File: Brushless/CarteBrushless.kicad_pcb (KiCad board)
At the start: 2 copper layers, 60 x 64 mm, 67 parts, among them J1 Conn_01x03_Pin, J2 Conn_01x03_Pin, J3 Conn_01x03_Pin, Q2 IRF7424, U1 STM32G484RETx, U2 TCAN332G

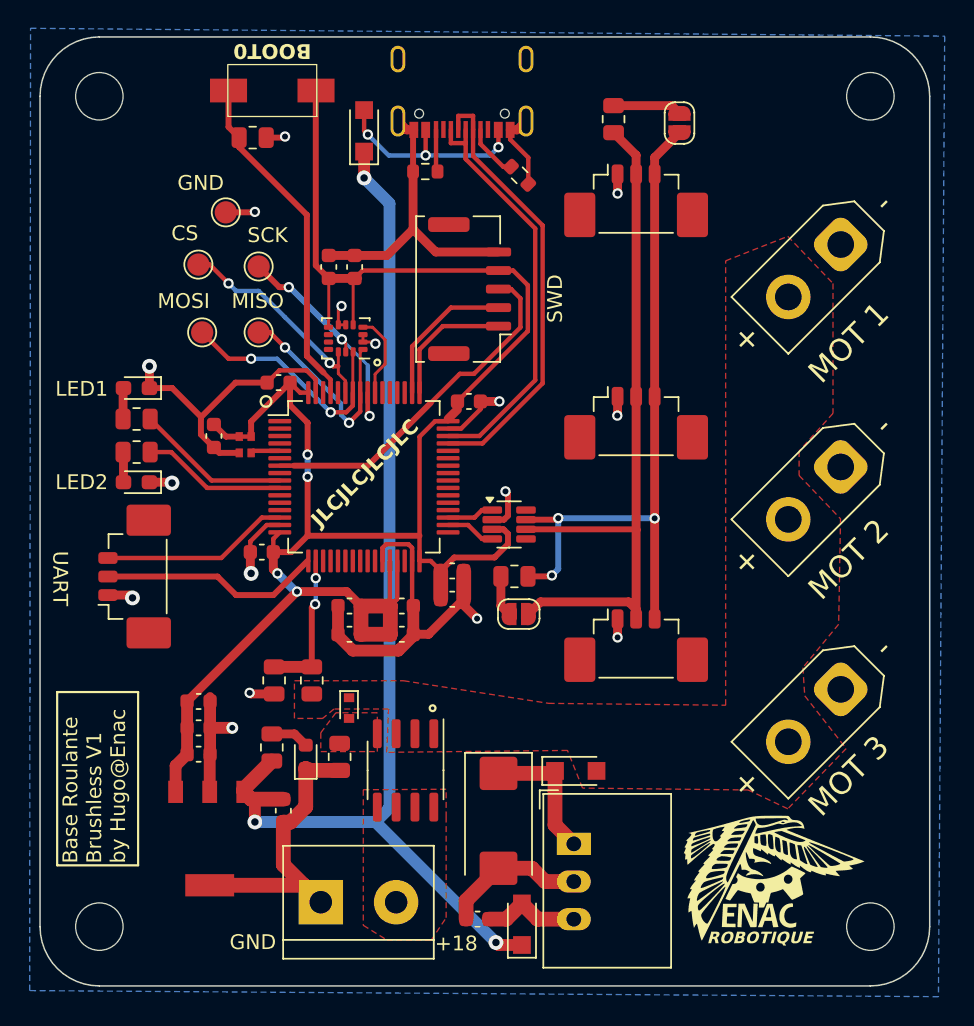
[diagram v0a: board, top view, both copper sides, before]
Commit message: change SWD footprint
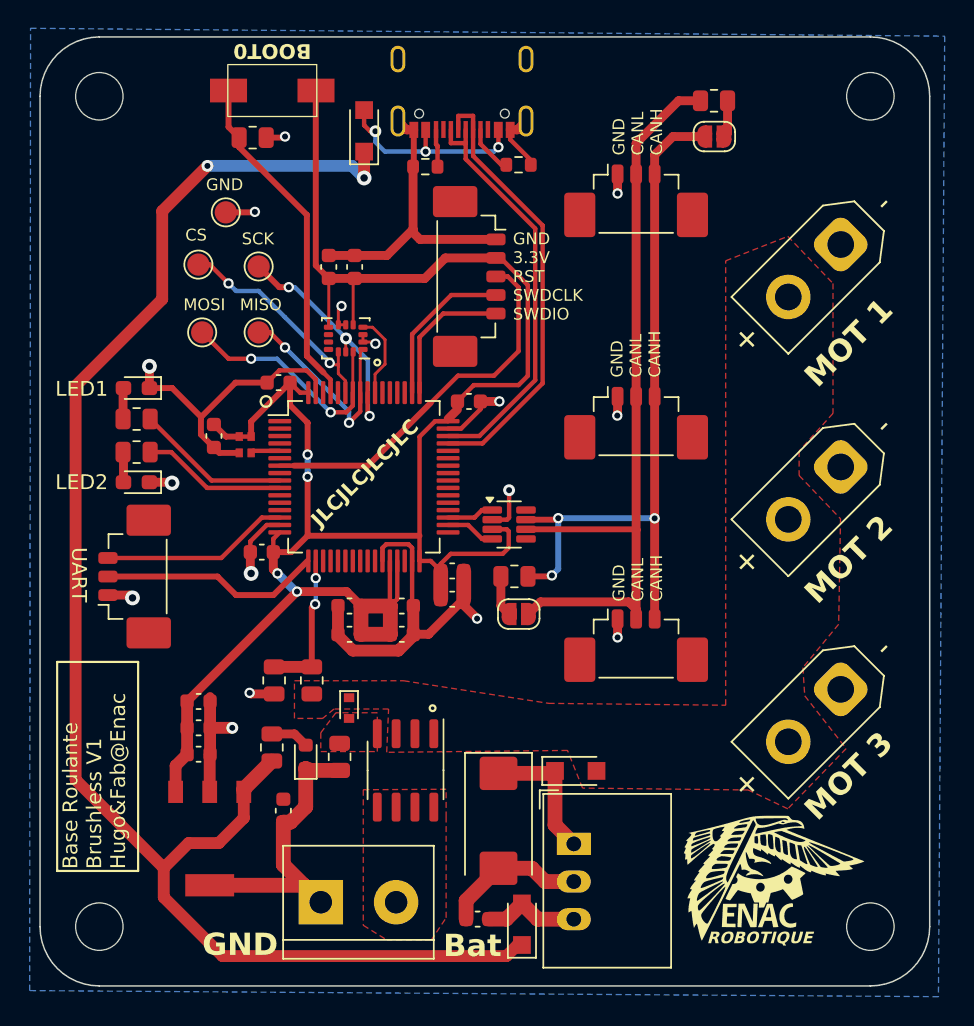
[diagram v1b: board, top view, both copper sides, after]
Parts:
- DEBUG1: footprint Connector_Molex:Molex_CLIK-Mate_502382-0570_1x05-1MP_P1.25mm_Vertical -> Connector_Molex:Molex_PicoBlade_53398-0571_1x05-1MP_P1.25mm_Vertical
- moved R11 6.89 mm to (141.5, 86.5), turned to 0 degrees
- moved JP2 2.52 mm to (141.5, 88.9), turned to 180 degrees
- moved DEBUG1 1.00 mm to (125.5, 98.3), turned to -90 degrees
- moved R7 0.71 mm to (128.3, 90.8), turned to 0 degrees
- moved R8 0.33 mm to (122.0, 90.9)
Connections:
- DEBUG1 pad 1: SWDIO -> GND
- DEBUG1 pad 2: SWCLK -> +3.3V
- DEBUG1 pad 4: +3.3V -> SWCLK
- DEBUG1 pad 5: GND -> SWDIO
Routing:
- net +5V: track 75.1 -> 105.7 mm, vias 3 -> 2
- net CAN_LOW: track 49.3 -> 53.5 mm
- net +3.3V: track 136.7 -> 139.5 mm
- net Net-(JP2-A): track 4.66 -> 2.51 mm
- net CAN_HIGH: track 47.9 -> 49.6 mm
- net RST: track 23.8 -> 25.4 mm
- net GND: track 138.1 -> 136.7 mm
- net SWDIO: track 8.89 -> 9.55 mm
- net SWCLK: track 10.0 -> 10.7 mm
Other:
- board text added: "3.3V"
- board text added: "Base Roulante Brushless V1 Edition 2025 by Hugo&Fab@Enac"
- board text added: "Base Roulante Brushless V1 Hugo&Fab@Enac"
- board text added: "Bat"
- board text added: "CANH"
- board text added: "CANL"
- board text added: "RST"
- board text added: "SWDCLK"
- board text added: "SWDIO"
- board text removed: "+18"
- board text removed: "Base Roulante Brushless V1 Edition 2025 by Hugo@Enac"
- board text removed: "Base Roulante Brushless V1 by Hugo@Enac"
- board text removed: "SWD"

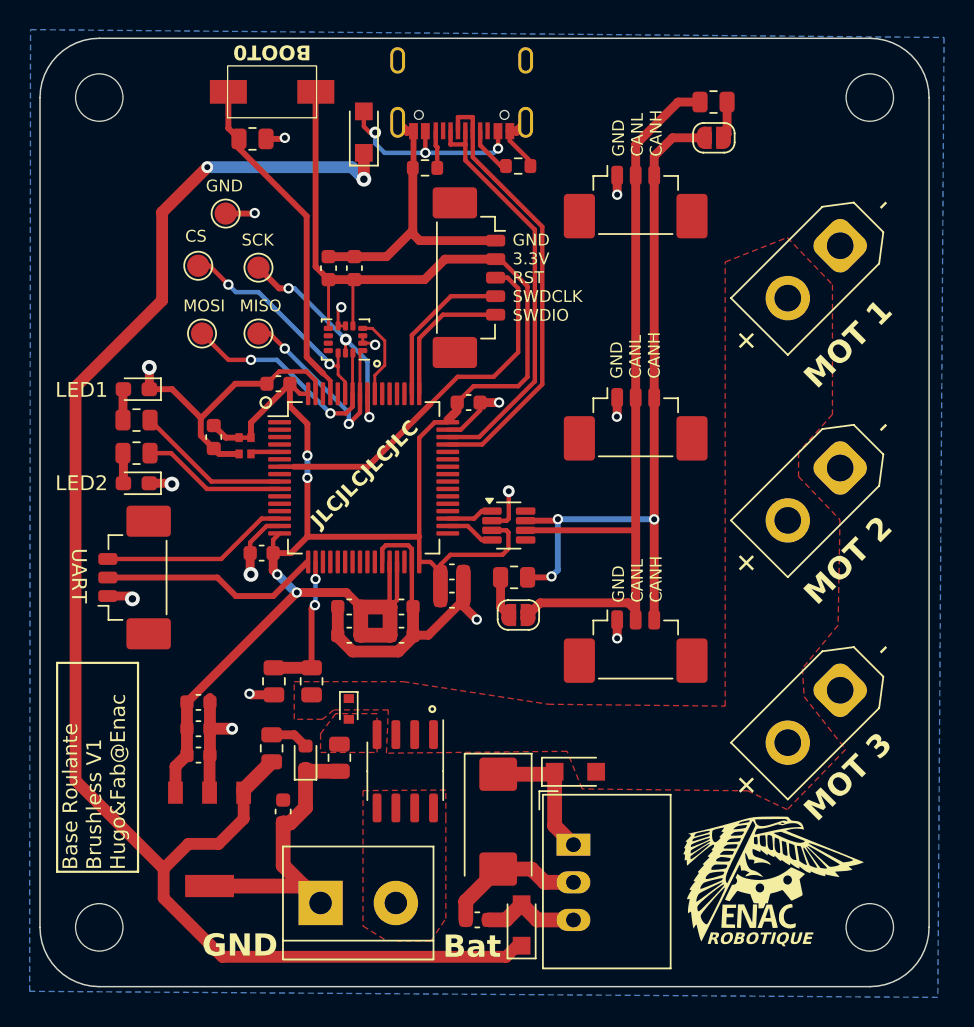
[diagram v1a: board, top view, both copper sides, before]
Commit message: Reduce mounting holes spacing
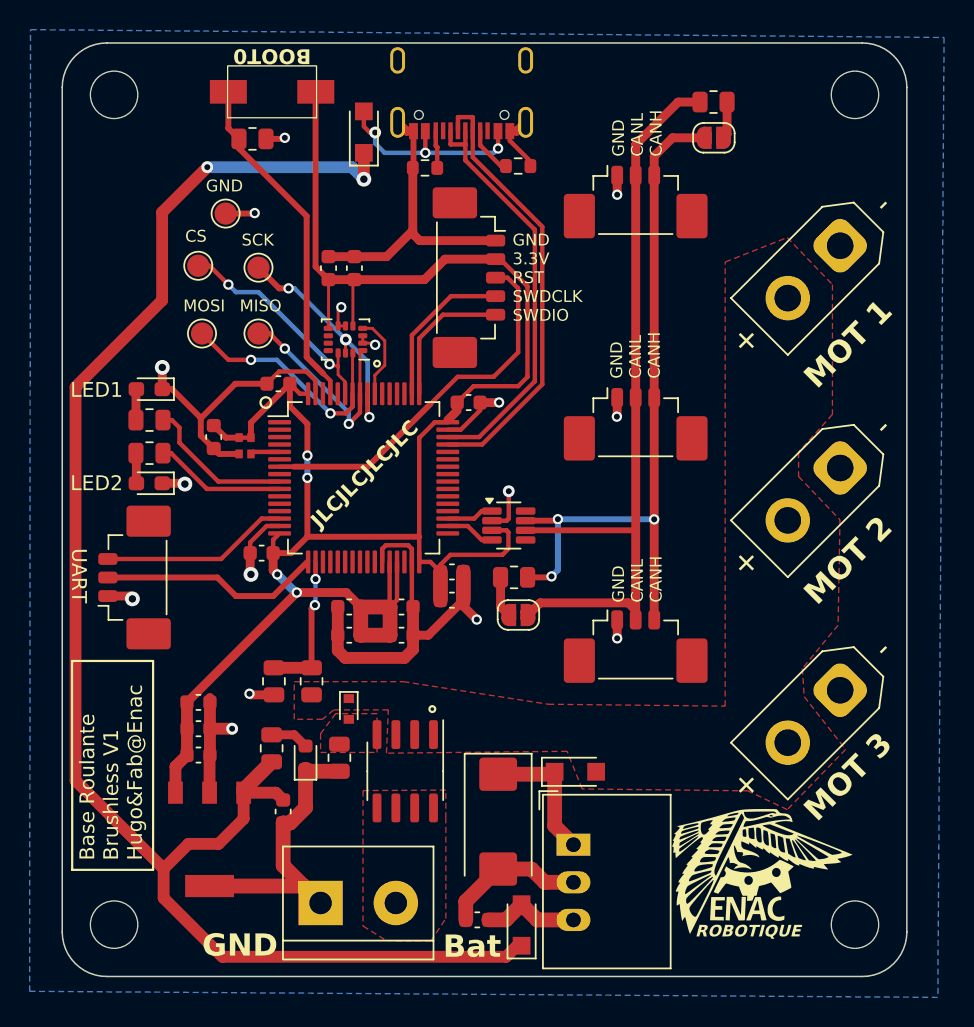
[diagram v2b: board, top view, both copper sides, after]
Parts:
- moved H1 1.02 mm to (101.0, 86.0)
- moved H2 1.02 mm to (151.0, 86.0)
- moved H3 1.02 mm to (151.0, 142.0)
- moved H4 1.02 mm to (101.0, 142.0)
- moved G*** 0.92 mm to (143.8, 138.2)
- moved LED1 0.88 mm to (103.4, 105.9)
- moved LED2 0.88 mm to (103.4, 112.2)
- moved R10 0.88 mm to (103.4, 108.0)
- moved R6 0.88 mm to (103.4, 110.2)
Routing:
- net +5V: track 105.7 -> 108.6 mm
- net LED2: track 9.74 -> 8.87 mm
- net GND: track 136.7 -> 137.2 mm
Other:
- board size 60 x 64 mm -> 57 x 63 mm

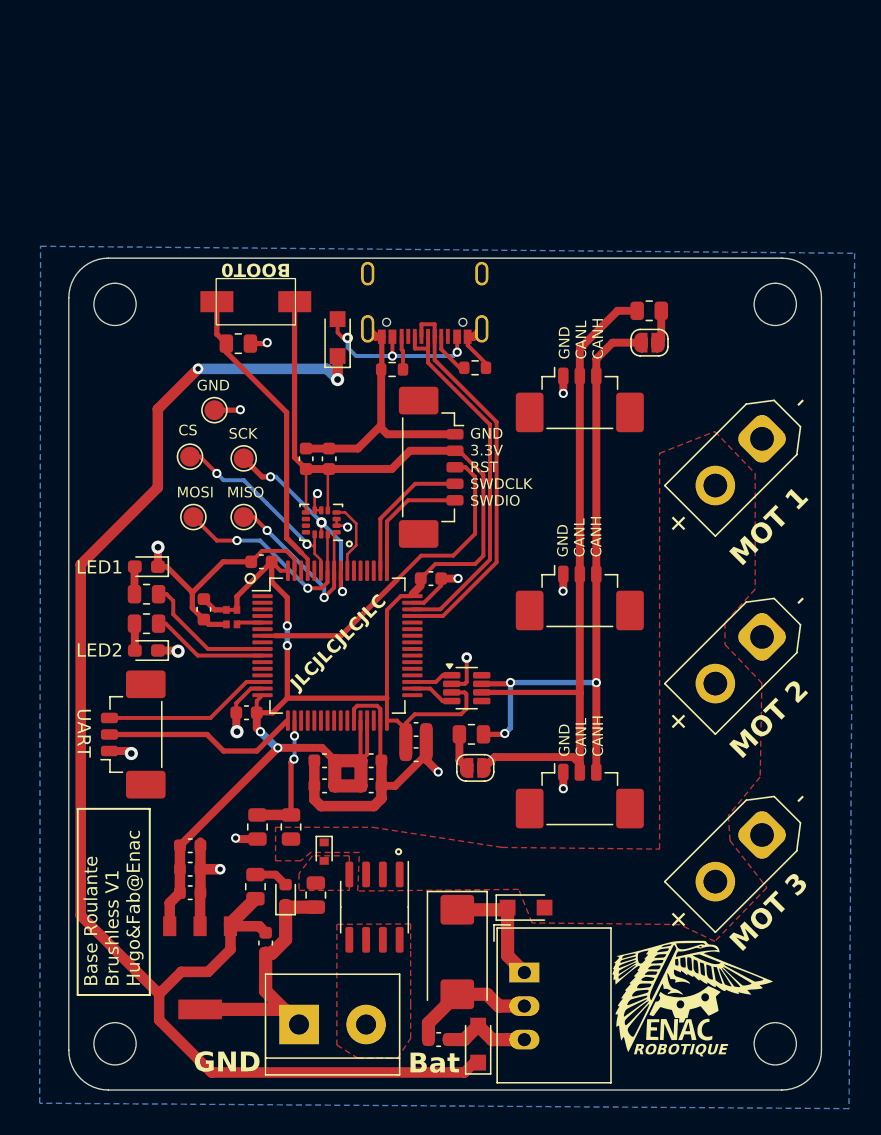
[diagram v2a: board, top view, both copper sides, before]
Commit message: Ajustement des trous
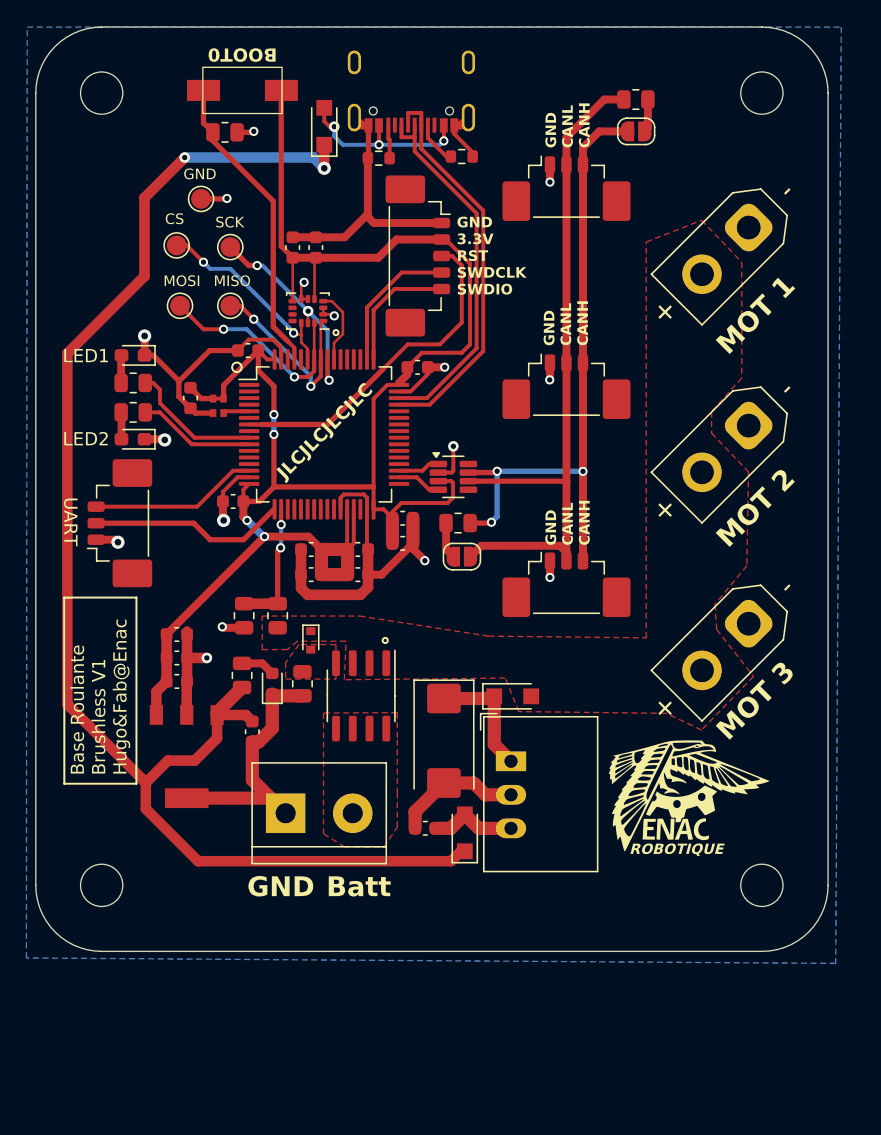
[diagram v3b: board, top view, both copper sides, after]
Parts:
- moved C19 16.0 mm to (111.4, 118.4)
- moved C22 16.0 mm to (105.7, 114.6)
- moved Transfo18->5 16.0 mm to (131.0, 120.6)
- moved Transfo5->3.3 16.0 mm to (106.4, 120.2)
- moved C10 16.0 mm to (111.1, 89.5)
- moved C11 16.0 mm to (122.8, 104.1)
- moved C12 16.0 mm to (119.4, 106.5)
- moved C13 16.0 mm to (119.4, 104.6)
- moved C14 16.0 mm to (115.9, 106.5)
- moved C15 16.0 mm to (115.9, 104.6)
- moved C16 16.0 mm to (114.5, 81.7)
- moved C17 16.0 mm to (116.2, 81.7)
- moved C18 16.0 mm to (106.7, 93.1)
- moved C20 16.0 mm to (105.7, 111.0)
- moved C23 16.0 mm to (125.9, 119.0)
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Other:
- board size 57 x 63 mm -> 60 x 70 mm
- board text added: "Batt"
- board text removed: "Bat"

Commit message: UART
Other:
- board text added: "RX"
- board text added: "TX"
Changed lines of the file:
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@@
 			(outputformat 1)
 			(mirror no)
-			(drillshape 1)
+			(drillshape 0)
 			(scaleselection 1)
 			(outputdirectory "")
@@
 	)
 	(gr_text "UART"
-		(at 97.032678 100.586 -90)
+		(at 95.5 100 0)
 		(layer "F.SilkS")
 		(effects
@@
 		)
 	)
+	(gr_text "RX"
+		(at 96 103.5 0)
+		(layer "F.SilkS")
+		(effects
+			(font
+				(size 1 1)
+				(thickness 0.15)
+			)
+			(justify left bottom)
+		)
+	)
 	(gr_text "MOT 3"
 		(at 149.524212 116.018466 45)
@@
 		)
 	)
+	(gr_text "TX"
+		(at 96 102 0)
+		(layer "F.SilkS")
+		(effects
+			(font
+				(size 1 1)
+				(thickness 0.15)
+			)
+			(justify left bottom)
+		)
+	)
 	(gr_text "CANL"
 		(at 135.767678 74.17 90)
@@
 			)
 			(justify left bottom)
+		)
+	)
+	(gr_text "GND"
+		(at 95.5 105 0)
+		(layer "F.SilkS")
+		(effects
+			(font
+				(size 1 1)
+				(thickness 0.15)
+			)
+			(justify left bottom)

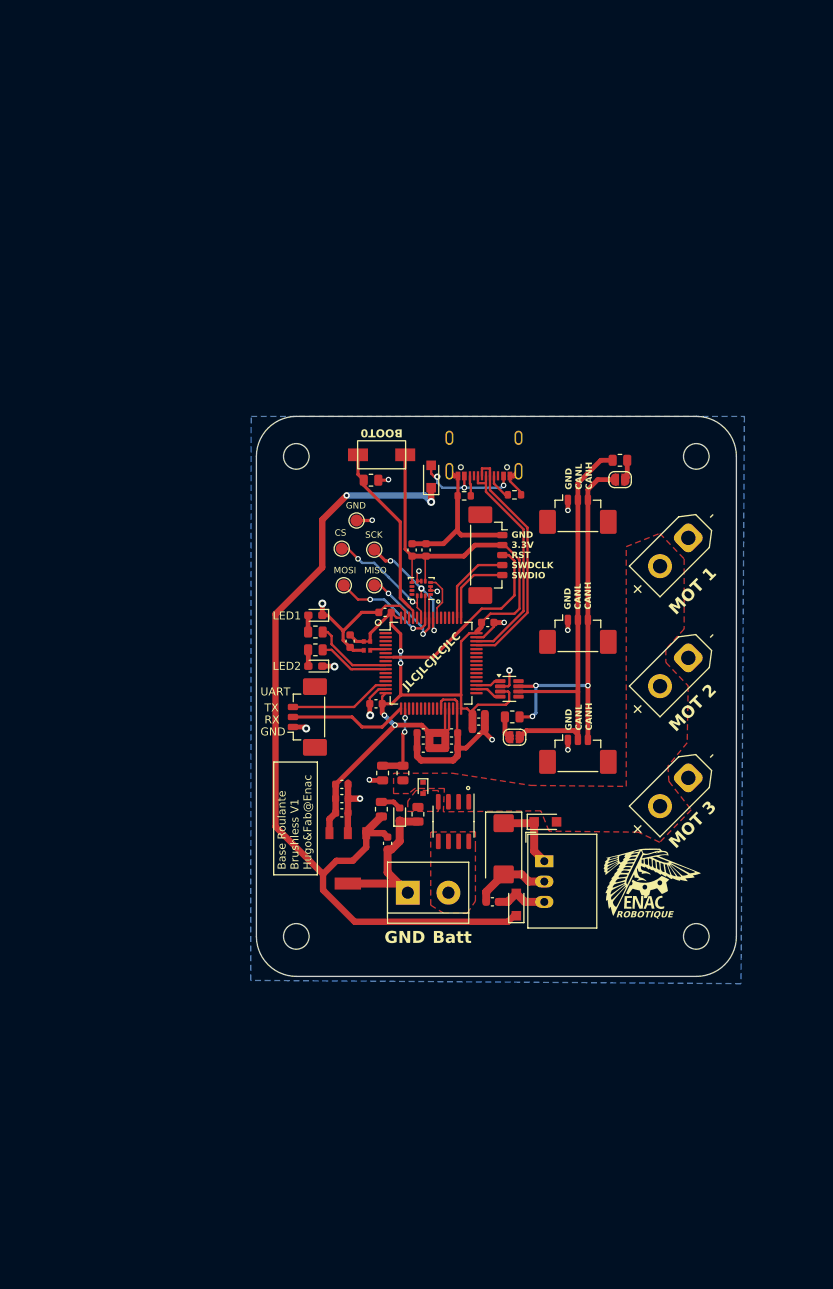
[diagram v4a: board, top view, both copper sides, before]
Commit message: save stencil
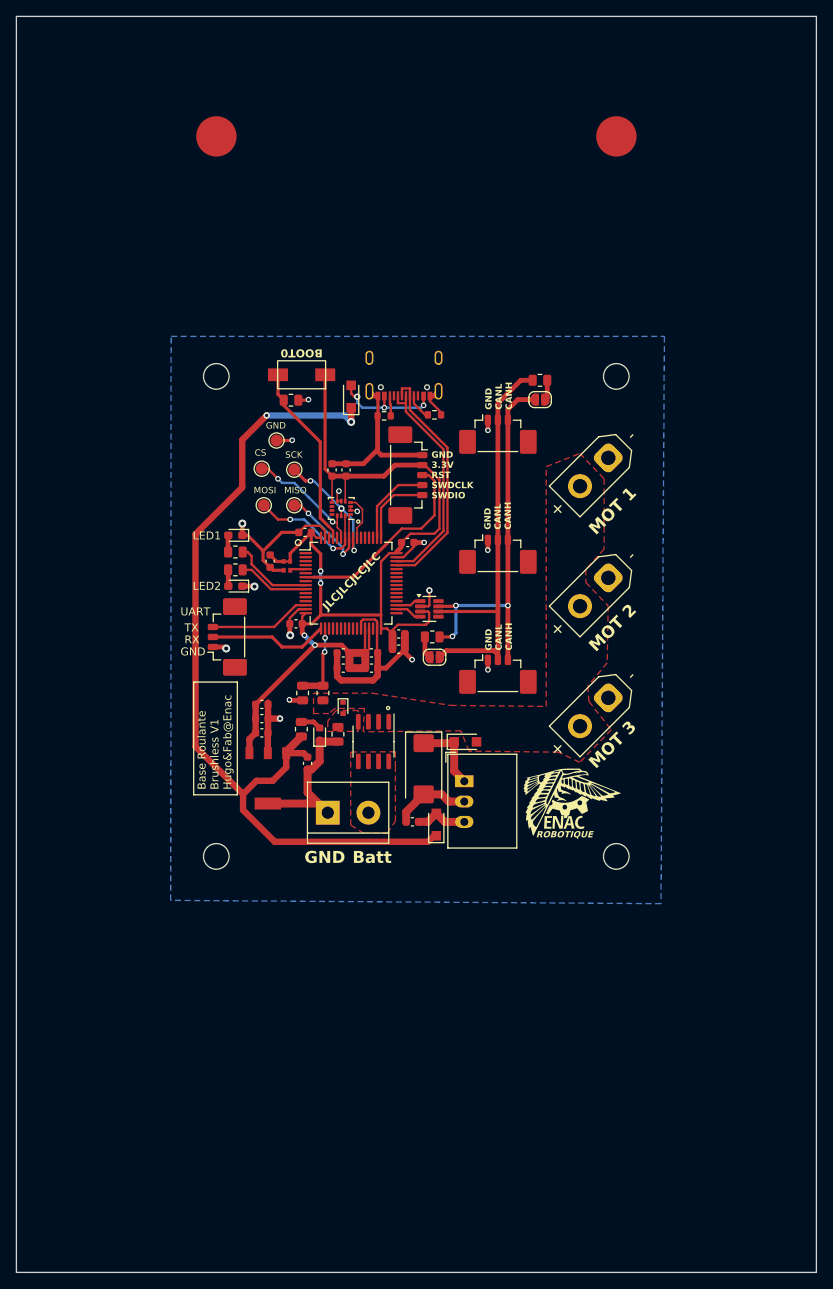
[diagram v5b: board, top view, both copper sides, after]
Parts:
- added REF**: EC-Registration, ENAC_robotique:EC-Registration, F.Cu at (90.0, 30.0)
- added REF**: EC-Registration, ENAC_robotique:EC-Registration, F.Cu at (140.0, 30.0)
- moved J1 14.1 mm to (125.2, 66.7)
- moved J2 14.1 mm to (125.2, 81.7)
- moved J3 14.1 mm to (125.2, 96.7)
- moved D3 14.1 mm to (106.8, 62.5)
- moved JP2 14.1 mm to (130.5, 62.9)
- moved ALIM1 14.1 mm to (103.9, 114.5)
- moved C10 14.1 mm to (101.1, 79.5)
- moved C11 14.1 mm to (112.8, 94.1)
- moved C12 14.1 mm to (109.4, 96.5)
- moved C13 14.1 mm to (109.4, 94.6)
- moved C14 14.1 mm to (105.9, 96.5)
- moved C15 14.1 mm to (105.9, 94.6)
- moved C16 14.1 mm to (104.5, 71.7)
- moved C17 14.1 mm to (106.2, 71.7)
- moved C18 14.1 mm to (96.7, 83.1)
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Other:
- board size 60 x 70 mm -> 100 x 157 mm
